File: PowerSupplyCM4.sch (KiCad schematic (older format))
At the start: 60 parts, among them J7 BAT, J8 IGNITION, Q1 NVMFS5C442NL, Q2 SQ2362ES-T1_GE3, Q3 SQD50P06-15L_GE3, Q4 SQJ461EP-T1-GE3, U10 VOMA617A, U11 VOMA617A, U12 LM53635LQRNL*Q1, U13 TLVH431AQDBVRQ1, U14 LM74610-Q1

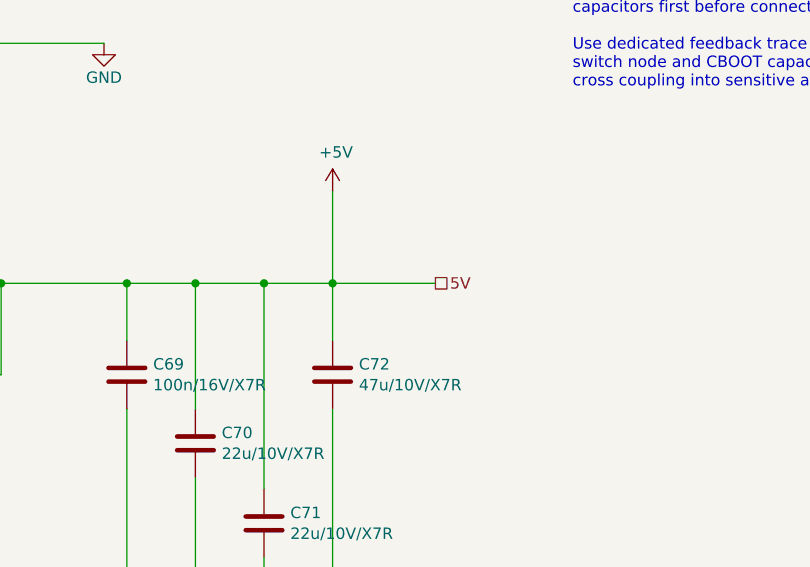
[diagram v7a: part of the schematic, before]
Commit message: - Platzoptimierungen
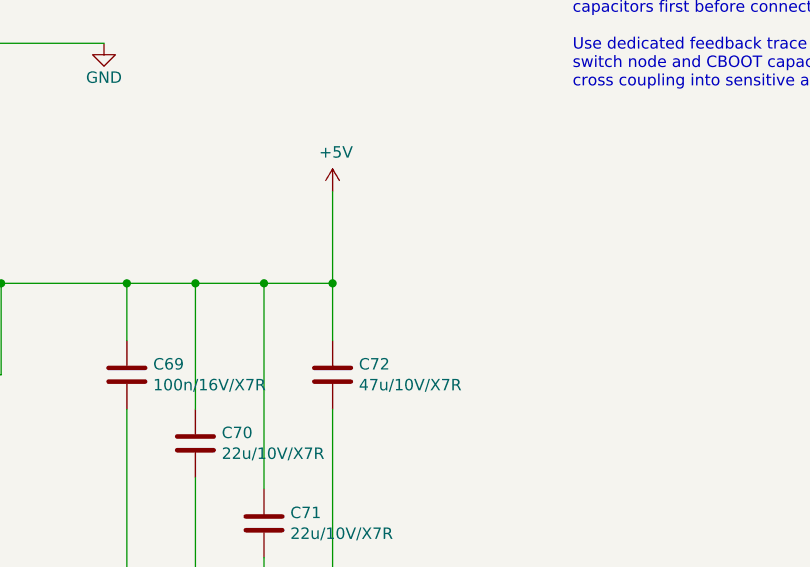
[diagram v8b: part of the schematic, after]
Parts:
- C67, C69: footprint Capacitor_SMD:C_0603_1608Metric -> Capacitor_SMD:C_0402_1005Metric
- C70, C71: footprint Capacitor_SMD:C_1206_3216Metric -> Capacitor_SMD:C_0805_2012Metric
- R22, R23, R24, R25, R26, R27, R28, R29, R30, R31, R32: footprint Resistor_SMD:R_0603_1608Metric -> Resistor_SMD:R_0402_1005Metric
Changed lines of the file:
@@
 $Descr A2 23386 16535
 encoding utf-8
-Sheet 8 9
+Sheet 3 9
 Title "TIDA-00746-SchDoc"
 Date "05 06 2020"
@@
 $EndComp
 Connection ~ 4000 4000
-Text HLabel 11550 8350 2    50   UnSpc ~ 0
-5V
 Wire Wire Line
 	6200 2800 6300 2800
@@
 F 0 "R26" H 7870 5146 50  0000 L CNN
 F 1 "30k1/1%" H 7870 5055 50  0000 L CNN
-F 2 "Resistor_SMD:R_0603_1608Metric" V 7730 5100 50  0001 C CNN
+F 2 "Resistor_SMD:R_0402_1005Metric" V 7730 5100 50  0001 C CNN
 F 3 "~" H 7800 5100 50  0001 C CNN
 	1    7800 5100
@@
 F 0 "R27" H 7870 5696 50  0000 L CNN
 F 1 "2k/1%" H 7870 5605 50  0000 L CNN
-F 2 "Resistor_SMD:R_0603_1608Metric" V 7730 5650 50  0001 C CNN
+F 2 "Resistor_SMD:R_0402_1005Metric" V 7730 5650 50  0001 C CNN
 F 3 "~" H 7800 5650 50  0001 C CNN
 	1    7800 5650
@@
 F 0 "R29" H 8370 5146 50  0000 L CNN
 F 1 "20k/1%" H 8370 5055 50  0000 L CNN
-F 2 "Resistor_SMD:R_0603_1608Metric" V 8230 5100 50  0001 C CNN
+F 2 "Resistor_SMD:R_0402_1005Metric" V 8230 5100 50  0001 C CNN
 F 3 "~" H 8300 5100 50  0001 C CNN
 	1    8300 5100
@@
 F 0 "R31" H 10970 2846 50  0000 L CNN
 F 1 "100k/1%" H 10970 2755 50  0000 L CNN
-F 2 "Resistor_SMD:R_0603_1608Metric" V 10830 2800 50  0001 C CNN
+F 2 "Resistor_SMD:R_0402_1005Metric" V 10830 2800 50  0001 C CNN
 F 3 "~" H 10900 2800 50  0001 C CNN
 	1    10900 2800
@@
 F 0 "R30" H 10770 5546 50  0000 L CNN
 F 1 "100k/1%" H 10770 5455 50  0000 L CNN
-F 2 "Resistor_SMD:R_0603_1608Metric" V 10630 5500 50  0001 C CNN
+F 2 "Resistor_SMD:R_0402_1005Metric" V 10630 5500 50  0001 C CNN
 F 3 "~" H 10700 5500 50  0001 C CNN
 	1    10700 5500
@@
 F 0 "C67" H 8115 9646 50  0000 L CNN
 F 1 "100n/16V/X7R" H 8115 9555 50  0000 L CNN
-F 2 "Capacitor_SMD:C_0603_1608Metric" H 8038 9450 50  0001 C CNN
+F 2 "Capacitor_SMD:C_0402_1005Metric" H 8038 9450 50  0001 C CNN
 F 3 "~" H 8000 9600 50  0001 C CNN
 	1    8000 9600
@@
 F 0 "C69" H 10315 8796 50  0000 L CNN
 F 1 "100n/16V/X7R" H 10315 8705 50  0000 L CNN
-F 2 "Capacitor_SMD:C_0603_1608Metric" H 10238 8600 50  0001 C CNN
+F 2 "Capacitor_SMD:C_0402_1005Metric" H 10238 8600 50  0001 C CNN
 F 3 "~" H 10200 8750 50  0001 C CNN
 	1    10200 8750
@@
 F 0 "C70" H 10615 9096 50  0000 L CNN
 F 1 "22u/10V/X7R" H 10615 9005 50  0000 L CNN
-F 2 "Capacitor_SMD:C_1206_3216Metric" H 10538 8900 50  0001 C CNN
+F 2 "Capacitor_SMD:C_0805_2012Metric" H 10538 8900 50  0001 C CNN
 F 3 "~" H 10500 9050 50  0001 C CNN
 	1    10500 9050
@@
 F 0 "C71" H 10915 9446 50  0000 L CNN
 F 1 "22u/10V/X7R" H 10915 9355 50  0000 L CNN
-F 2 "Capacitor_SMD:C_1206_3216Metric" H 10838 9250 50  0001 C CNN
+F 2 "Capacitor_SMD:C_0805_2012Metric" H 10838 9250 50  0001 C CNN
 F 3 "~" H 10800 9400 50  0001 C CNN
 	1    10800 9400
@@
 F 0 "R32" H 11570 3396 50  0000 L CNN
 F 1 "20k/5%" H 11570 3305 50  0000 L CNN
-F 2 "Resistor_SMD:R_0603_1608Metric" V 11430 3350 50  0001 C CNN
+F 2 "Resistor_SMD:R_0402_1005Metric" V 11430 3350 50  0001 C CNN
 F 3 "~" H 11500 3350 50  0001 C CNN
 	1    11500 3350
@@
 F 0 "R22" H 5370 9796 50  0000 L CNN
 F 1 "100k/5%" H 5370 9705 50  0000 L CNN
-F 2 "Resistor_SMD:R_0603_1608Metric" V 5230 9750 50  0001 C CNN
+F 2 "Resistor_SMD:R_0402_1005Metric" V 5230 9750 50  0001 C CNN
 F 3 "~" H 5300 9750 50  0001 C CNN
 	1    5300 9750
@@
 Connection ~ 9500 8350
 Wire Wire Line
-	11100 8350 11550 8350
-Wire Wire Line
 	9650 8350 10200 8350
 Wire Wire Line
@@
 F 0 "R28" V 7643 13700 50  0000 C CNN
 F 1 "10k/1%" V 7734 13700 50  0000 C CNN
-F 2 "Resistor_SMD:R_0603_1608Metric" V 7780 13700 50  0001 C CNN
+F 2 "Resistor_SMD:R_0402_1005Metric" V 7780 13700 50  0001 C CNN
 F 3 "~" H 7850 13700 50  0001 C CNN
 	1    7850 13700
@@
 F 0 "R24" V 6143 13700 50  0000 C CNN
 F 1 "10k/1%" V 6234 13700 50  0000 C CNN
-F 2 "Resistor_SMD:R_0603_1608Metric" V 6280 13700 50  0001 C CNN
+F 2 "Resistor_SMD:R_0402_1005Metric" V 6280 13700 50  0001 C CNN
 F 3 "~" H 6350 13700 50  0001 C CNN
 	1    6350 13700
@@
 F 0 "R25" V 6343 13700 50  0000 C CNN
 F 1 "10k/1%" V 6434 13700 50  0000 C CNN
-F 2 "Resistor_SMD:R_0603_1608Metric" V 6480 13700 50  0001 C CNN
+F 2 "Resistor_SMD:R_0402_1005Metric" V 6480 13700 50  0001 C CNN
 F 3 "~" H 6550 13700 50  0001 C CNN
 	1    6550 13700
@@
 F 0 "R23" V 5843 15000 50  0000 C CNN
 F 1 "10k/1%" V 5934 15000 50  0000 C CNN
-F 2 "Resistor_SMD:R_0603_1608Metric" V 5980 15000 50  0001 C CNN
+F 2 "Resistor_SMD:R_0402_1005Metric" V 5980 15000 50  0001 C CNN
 F 3 "~" H 6050 15000 50  0001 C CNN
 	1    6050 15000
